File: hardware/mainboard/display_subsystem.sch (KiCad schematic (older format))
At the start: 0 parts

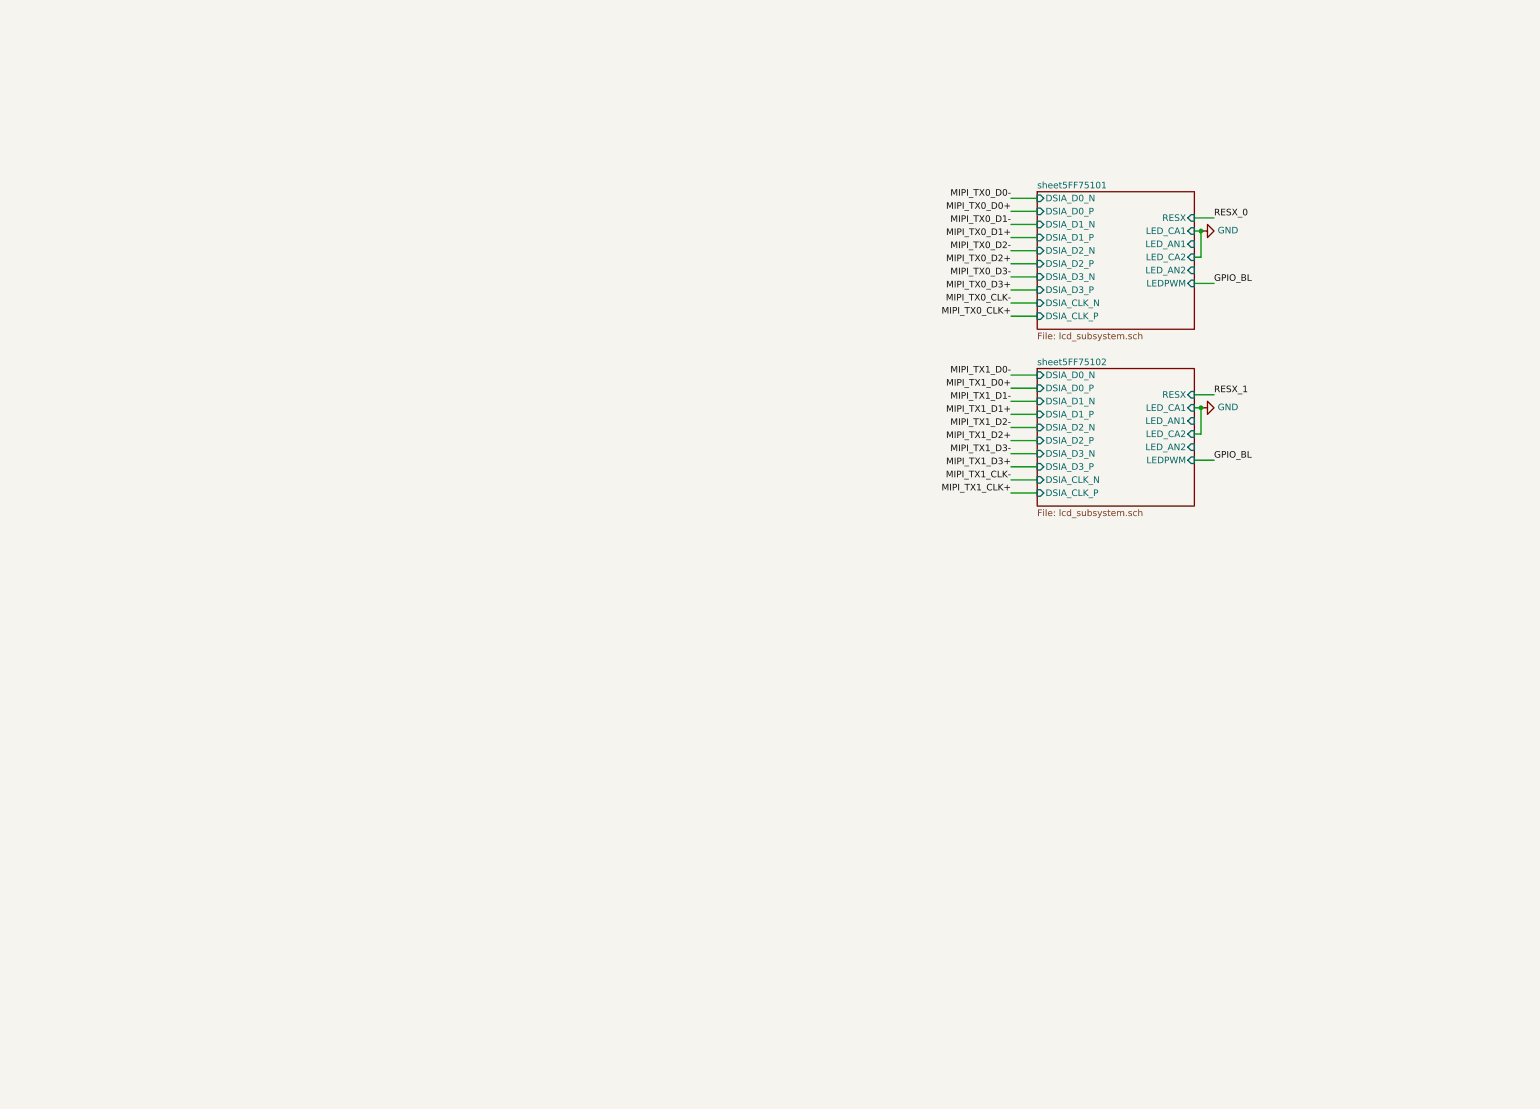
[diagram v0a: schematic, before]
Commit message: finish sch arch, remove coproc, add bl driver, need to do TC power supply
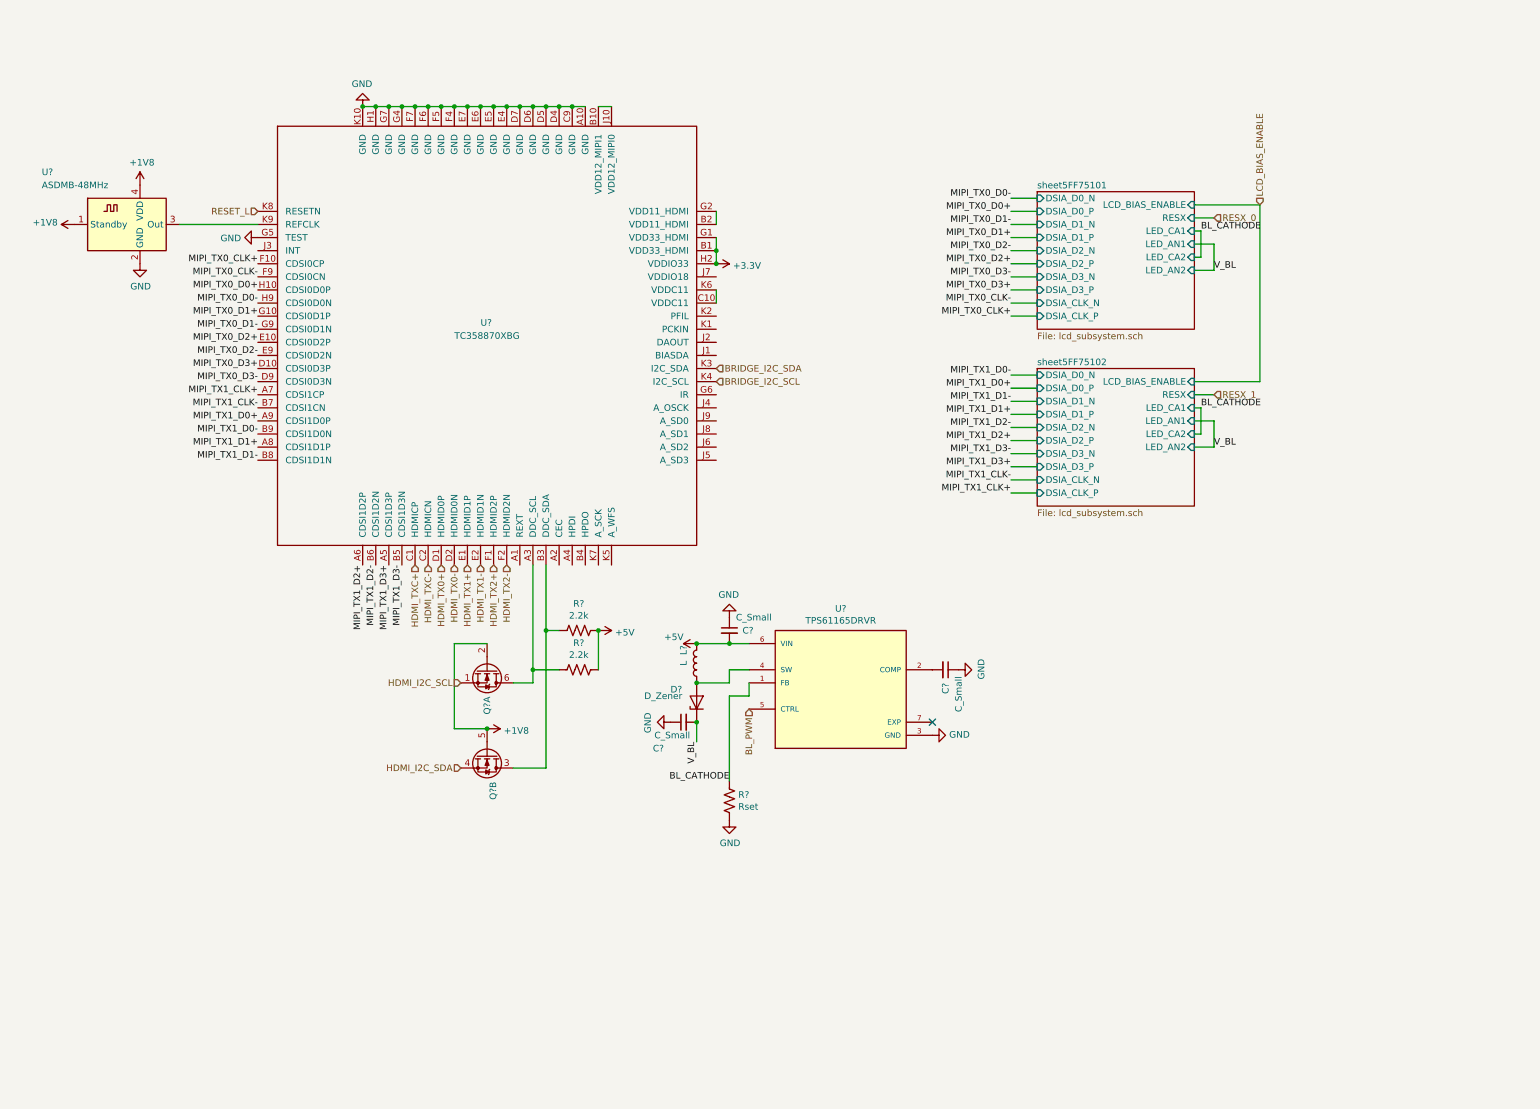
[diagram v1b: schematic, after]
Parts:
- added C? (x3): C_Small, symbol Device:C_Small
- added D?: D_Zener, symbol Device:D_Zener
- added L?: L, symbol Device:L
- added Q? (x2): FDG1024NZ, Package_TO_SOT_SMD:SOT-363_SC-70-6, symbol Transistor_FET:FDG1024NZ
- added R? (x2): 2.2k, symbol Device:R_US
- added R?: Rset, symbol Device:R_US
- added U?: TC358870XBG, symbol mainboard:TC358870XBG
- added U?: TPS61165DRVR, SON65P200X200X80-7N, symbol mainboard:TPS61165DRVR
- added U?: ASDMB-48MHz, Oscillator:Oscillator_SMD_Abracon_ASDMB-4Pin_2.5x2.0mm, symbol Oscillator:ASDMB-xxxMHz
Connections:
- net GND: now also C?.1, C?.1, C?.1, R?.1, U?.2 (GND), U?.3 (GND), U?.A10 (GND), U?.C9 (GND), U?.D4 (GND), U?.D5 (GND), U?.D6 (GND), U?.D7 (GND), U?.E4 (GND), U?.E5 (GND), U?.E6 (GND), U?.E7 (GND), U?.F4 (GND), U?.F5 (GND), U?.F6 (GND), U?.F7 (GND), U?.G4 (GND), U?.G5 (TEST), U?.G7 (GND), U?.H1 (GND), U?.K10 (GND)
- net MIPI_TX0_CLK+: now also U?.F10 (CDSI0CP)
- net MIPI_TX0_CLK-: now also U?.F9 (CDSI0CN)
- net MIPI_TX0_D0+: now also U?.H10 (CDSI0D0P)
- net MIPI_TX0_D0-: now also U?.H9 (CDSI0D0N)
- net MIPI_TX0_D1+: now also U?.G10 (CDSI0D1P)
- net MIPI_TX0_D1-: now also U?.G9 (CDSI0D1N)
- net MIPI_TX0_D2+: now also U?.E10 (CDSI0D2P)
- net MIPI_TX0_D2-: now also U?.E9 (CDSI0D2N)
- net MIPI_TX0_D3+: now also U?.D10 (CDSI0D3P)
- net MIPI_TX0_D3-: now also U?.D9 (CDSI0D3N)
- net MIPI_TX1_CLK+: now also U?.A7 (CDSI1CP)
- net MIPI_TX1_CLK-: now also U?.B7 (CDSI1CN)
- net MIPI_TX1_D0+: now also U?.A9 (CDSI1D0P)
- net MIPI_TX1_D0-: now also U?.B9 (CDSI1D0N)
- net MIPI_TX1_D1+: now also U?.A8 (CDSI1D1P)
- net MIPI_TX1_D1-: now also U?.B8 (CDSI1D1N)
- net MIPI_TX1_D2+: now also U?.A6 (CDSI1D2P)
- net MIPI_TX1_D2-: now also U?.B6 (CDSI1D2N)
- net MIPI_TX1_D3+: now also U?.A5 (CDSI1D3P)
- net MIPI_TX1_D3-: now also U?.B5 (CDSI1D3N)
- new net: Q?.6 (D), R?.2, U?.A3 (DDC_SCL)
- new net: U?.B10 (VDD12_MIPI1), U?.J10 (VDD12_MIPI0)
- new net: U?.B2 (VDD11_HDMI), U?.G2 (VDD11_HDMI)
- new net: Q?.3 (D), R?.2, U?.B3 (DDC_SDA)
- new net: U?.C10 (VDDC11), U?.K6 (VDDC11)
- new net: U?.3 (Out), U?.K9 (REFCLK)
- new net: C?.2, U?.2 (COMP)
- new net: D?.2 (A), L?.1, U?.4 (SW)
- new net +1V8: Q?.2 (G), Q?.5 (G), U?.1 (Standby), U?.4 (VDD)
- new net +3V3: U?.B1 (VDD33_HDMI), U?.G1 (VDD33_HDMI), U?.H2 (VDDIO33)
- new net +5V: C?.2, L?.2, R?.1, R?.1, U?.6 (VIN)
- new net BL_CATHODE: R?.2, U?.1 (FB)
- new net BL_PWM: U?.5 (CTRL)
- new net BRIDGE_I2C_SCL: U?.K4 (I2C_SCL)
- new net BRIDGE_I2C_SDA: U?.K3 (I2C_SDA)
- new net HDMI_I2C_SCL: Q?.1 (S)
- new net HDMI_I2C_SDA: Q?.4 (S)
- new net HDMI_TX0+: U?.D1 (HDMID0P)
- new net HDMI_TX0-: U?.D2 (HDMID0N)
- new net HDMI_TX1+: U?.E1 (HDMID1P)
- new net HDMI_TX1-: U?.E2 (HDMID1N)
- new net HDMI_TX2+: U?.F1 (HDMID2P)
- new net HDMI_TX2-: U?.F2 (HDMID2N)
- new net HDMI_TXC+: U?.C1 (HDMICP)
- new net HDMI_TXC-: U?.C2 (HDMICN)
- new net RESET_L: U?.K8 (RESETN)
- new net V_BL: C?.2, D?.1 (K)
- no-connect marks 0 -> 1

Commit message: finish basic schematic, need to decide audio situation
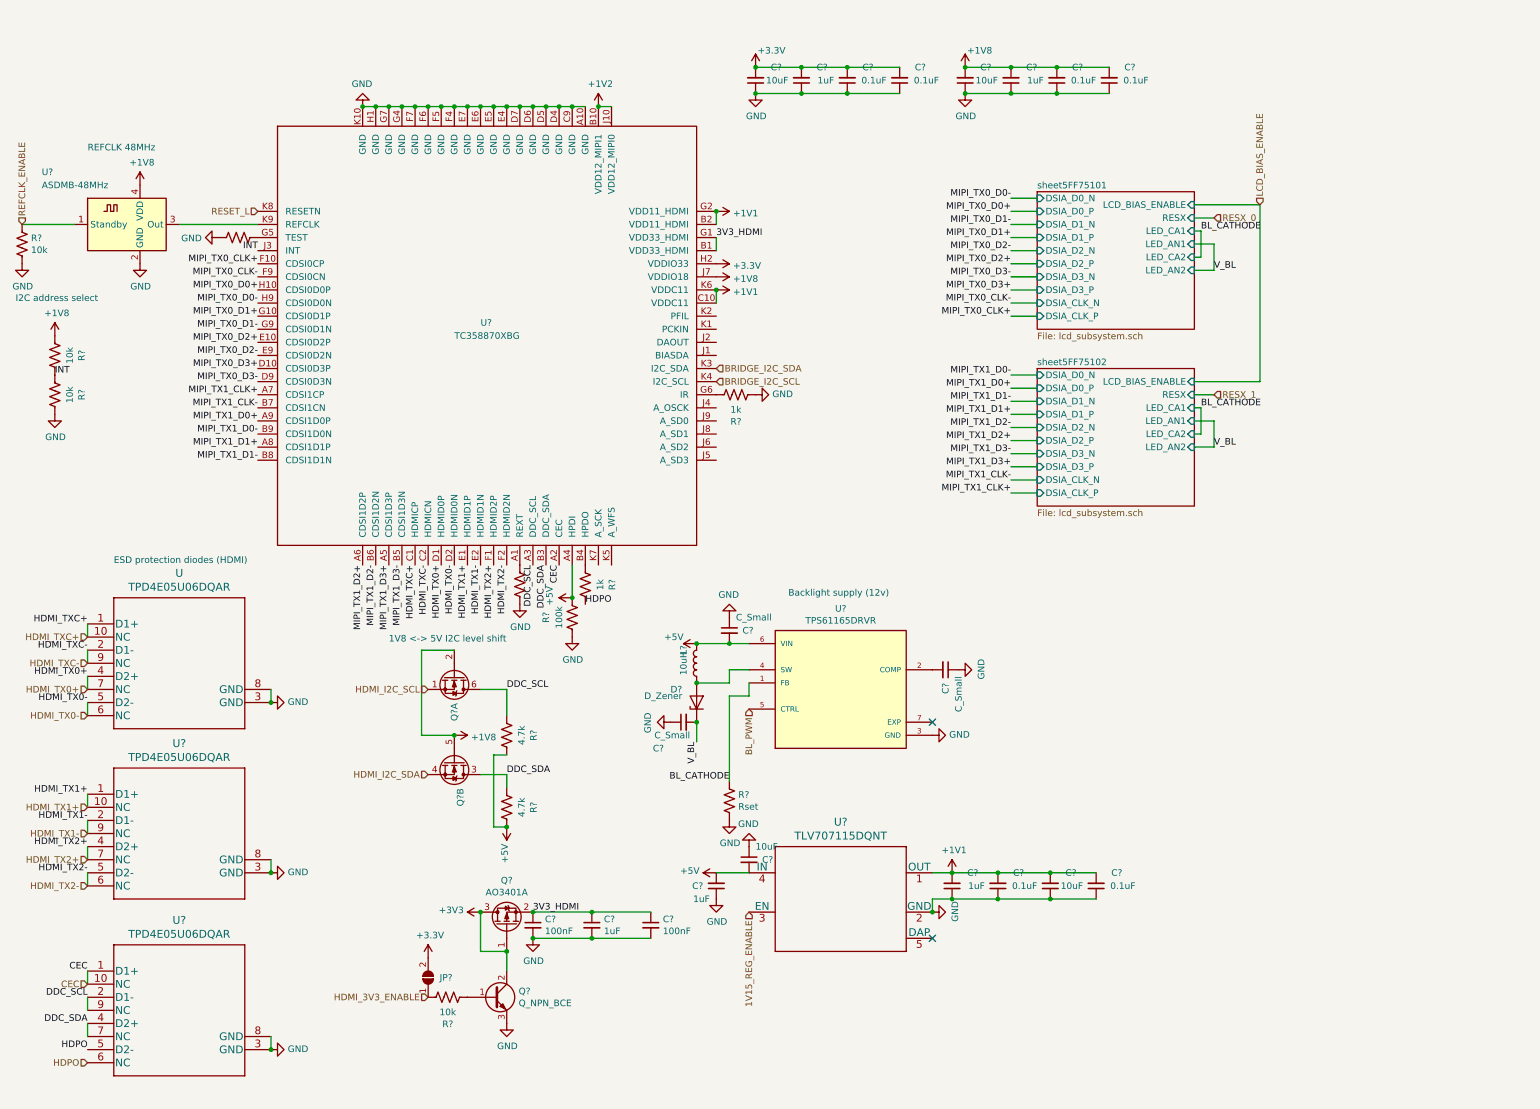
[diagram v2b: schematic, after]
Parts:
- added C? (x2): 100nF, symbol Device:C_Small
- added C? (x5): 1uF, symbol Device:C_Small
- added C? (x6): 0.1uF, symbol Device:C_Small
- added C? (x4): 10uF, symbol Device:C_Small
- added JP?: SolderJumper_2_Open, symbol Jumper:SolderJumper_2_Open
- added Q?: AO3401A, Package_TO_SOT_SMD:SOT-23, symbol Transistor_FET:AO3401A
- added Q?: Q_NPN_BCE, symbol Device:Q_NPN_BCE
- added R?: 2k, symbol Device:R_US
- added R? (x4): 10k, symbol Device:R_US
- added R?: 100k, symbol Device:R_US
- added R? (x3): 1k, symbol Device:R_US
- added U, U? (x2): TPD4E05U06DQAR, DQA0010A, symbol mainboard:TPD4E05U06DQAR
- added U?: TLV707115DQNT, DQN0004A, symbol mainboard:TLV707115DQNT
- L?: value L -> 10uH
- R? (x2): value 2.2k -> 4.7k
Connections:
- net +1V8: now also U?.J7 (VDDIO18), C?.2, C?.2, C?.2, C?.2, R?.2; no longer U?.1 (Standby)
- net +3V3: now also C?.2, C?.2, C?.2, C?.2, JP?.2 (B), Q?.1 (G), Q?.2 (C), Q?.3 (D); no longer U?.B1 (VDD33_HDMI), U?.G1 (VDD33_HDMI)
- net +5V: now also U?.A4 (HPDI), C?.2, C?.2, R?.2, U?.4 (IN)
- net GND: now also C?.1, C?.1, C?.1, C?.1, C?.1, C?.1, C?.1, C?.1, C?.1, C?.1, C?.1, C?.1, C?.1, C?.1, C?.2, C?.2, C?.2, Q?.3 (E), R?.1, R?.1, R?.2, R?.2, R?.2, R?.2, U.3 (GND), U.8 (GND), U?.2 (GND), U?.3 (GND), U?.3 (GND), U?.8 (GND), U?.8 (GND); no longer U?.G5 (TEST)
- net HDMI_TX0+: now also U.4 (D2+), U.7 (NC)
- net HDMI_TX0-: now also U.5 (D2-), U.6 (NC)
- net HDMI_TX1+: now also U?.1 (D1+), U?.10 (NC)
- net HDMI_TX1-: now also U?.2 (D1-), U?.9 (NC)
- net HDMI_TX2+: now also U?.4 (D2+), U?.7 (NC)
- net HDMI_TX2-: now also U?.5 (D2-), U?.6 (NC)
- net HDMI_TXC+: now also U.1 (D1+), U.10 (NC)
- net HDMI_TXC-: now also U.2 (D1-), U.9 (NC)
- net at U?.A1 (REXT): now also R?.1
- net CEC: now reaches U?.A2 (CEC)
- net CEC: now also U?.1 (D1+), U?.10 (NC)
- net DDC_SCL: now reaches Q?.6 (D), R?.2, U?.A3 (DDC_SCL)
- net DDC_SCL: now also U?.2 (D1-), U?.9 (NC)
- net +1V2: now reaches U?.B10 (VDD12_MIPI1), U?.J10 (VDD12_MIPI0)
- net +1V1: now reaches U?.B2 (VDD11_HDMI), U?.G2 (VDD11_HDMI)
- net +1V1: now also U?.C10 (VDDC11), U?.K6 (VDDC11), C?.2, C?.2, C?.2, C?.2, U?.1 (OUT)
- net DDC_SDA: now reaches Q?.3 (D), R?.2, U?.B3 (DDC_SDA)
- net DDC_SDA: now also U?.4 (D2+), U?.7 (NC)
- net at U?.B4 (HPDO): now also R?.2
- net at U?.G6 (IR): now also R?.1
- net INT: now reaches U?.J3 (INT)
- net INT: now also R?.1, R?.2
- new net: R?.1, U?.G5 (TEST)
- new net: Q?.1 (B), R?.2
- new net 1V15_REG_ENABLE: U?.3 (EN)
- new net 3V3_HDMI: C?.1, C?.1, C?.1, Q?.2 (S), U?.B1 (VDD33_HDMI), U?.G1 (VDD33_HDMI)
- new net HDMI_3V3_ENABLE: JP?.1 (A), R?.1
- new net HDPO: R?.1, U?.5 (D2-), U?.6 (NC)
- new net REFCLK_ENABLE: R?.1, U?.1 (Standby)
- no-connect marks 1 -> 2
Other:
- note added: "1V8 <-> 5V I2C level shift"
- note added: "Backlight supply (12v)"
- note added: "ESD protection diodes (HDMI)"
- note added: "I2C address select"
- note added: "REFCLK 48MHz\n"
- moved on the sheet: Q?A, Q?B, R?

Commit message: cleanup, audio pll, decide board layout
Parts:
- added C?: 10uF, symbol Device:C_Small
- added C? (x2): 1uF, symbol Device:C_Small
- added C?: 5pF, symbol Device:C_Small
- added C? (x4): 100nF, symbol Device:C_Small
- added C?: 1000pF, symbol Device:C_Small
- added L?: L_Core_Ferrite_Small, symbol Device:L_Core_Ferrite_Small
- added Q?: Q_NPN_BCE, symbol Device:Q_NPN_BCE
- added R? (x3): 33, symbol Device:R_US
- added R?: 10k, symbol Device:R_US
- added R?: 1.5k, symbol Device:R_US
- added R? (x2): 1k, symbol Device:R_US
- added TP? (x23): TestPoint, symbol Connector:TestPoint
- added U?: TC1014-1.8VCT713, SOT95P280X145-5N, symbol mainboard:TC1014-1.8VCT713
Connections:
- net +1V1: now also TP?.1
- net +1V8: no longer C?.2, C?.2, C?.2, C?.2, U?.J7 (VDDIO18)
- net +3V3: now also R?.2, R?.2, TP?.1; no longer C?.2, C?.2, C?.2, C?.2, Q?.1 (G), Q?.2 (C)
- net +5V: now also C?.2, C?.2, U?.1 (VIN)
- net 3V3_HDMI: now also C?.2, C?.2, C?.2, C?.2, C?.2, L?.2, TP?.1
- net BL_CATHODE: now also TP?.1
- net BRIDGE_I2C_SCL: now also TP?.1
- net BRIDGE_I2C_SDA: now also TP?.1
- net CEC: now also R?.2, TP?.1; no longer U?.A2 (CEC)
- net DDC_SCL: now also R?.1, TP?.1; no longer Q?.6 (D), R?.2
- net DDC_SDA: now also R?.1, TP?.1; no longer Q?.3 (D), R?.2
- net GND: now also U?.7 (EXP), C?.1, C?.1, C?.1, C?.1, C?.1, C?.1, C?.1, C?.2, R?.1, U?.2 (GND); no longer R?.2
- net HDMI_I2C_SCL: now also TP?.1
- net HDMI_I2C_SDA: now also TP?.1
- net HDPO: now also TP?.1
- net INT: now also TP?.1
- net LCD_BIAS_ENABLE: now also TP?.1
- net REFCLK_ENABLE: now also TP?.1
- net RESET_L: now also TP?.1
- net RESX_1: now also TP?.1
- net V_BL: now also TP?.1
- net BIASDA: now reaches U?.J1 (BIASDA)
- net BIASDA: now also C?.2
- net DAOUT: now reaches U?.J2 (DAOUT)
- net DAOUT: now also R?.2
- net PCKIN: now reaches U?.K1 (PCKIN)
- net PCKIN: now also C?.1
- net PFIL: now reaches U?.K2 (PFIL)
- net PFIL: now also C?.2, R?.2
- net at U?.3 (Out), U?.K9 (REFCLK): now also TP?.1
- net at Q?.1 (B), R?.2: now also TP?.1
- new net: R?.1, U?.A2 (CEC)
- new net: Q?.6 (D), R?.2, R?.2
- new net: Q?.3 (D), R?.2, R?.2
- new net: Q?.1 (G), Q?.2 (C), R?.1, TP?.1
- new net: C?.2, Q?.1 (B), R?.1
- new net: C?.2, L?.1, Q?.2 (C)
- new net: C?.2, Q?.3 (E), R?.2
- new net: C?.1, R?.1
- new net BRIDGE_1V8_REG_ENABLE: TP?.1, U?.3 (~SHDN)
- new net VDDIO18: C?.2, C?.2, C?.2, C?.2, TP?.1, U?.5 (VOUT), U?.J7 (VDDIO18)
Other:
- note added: "1.15v regulator"
- note added: "Audio PLL"
- note added: "Displays\n"
- note added: "HDMI PHY enable"
- note added: "Separate 1.8v regulator for HDMI bridge"
- moved on the sheet: C?, JP?, Q?, Q?A, Q?B, R?
